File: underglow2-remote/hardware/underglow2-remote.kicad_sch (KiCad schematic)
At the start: 2 parts, among them J101 AFC01-S40FCA-00, U101 ATGM332D-5NR32

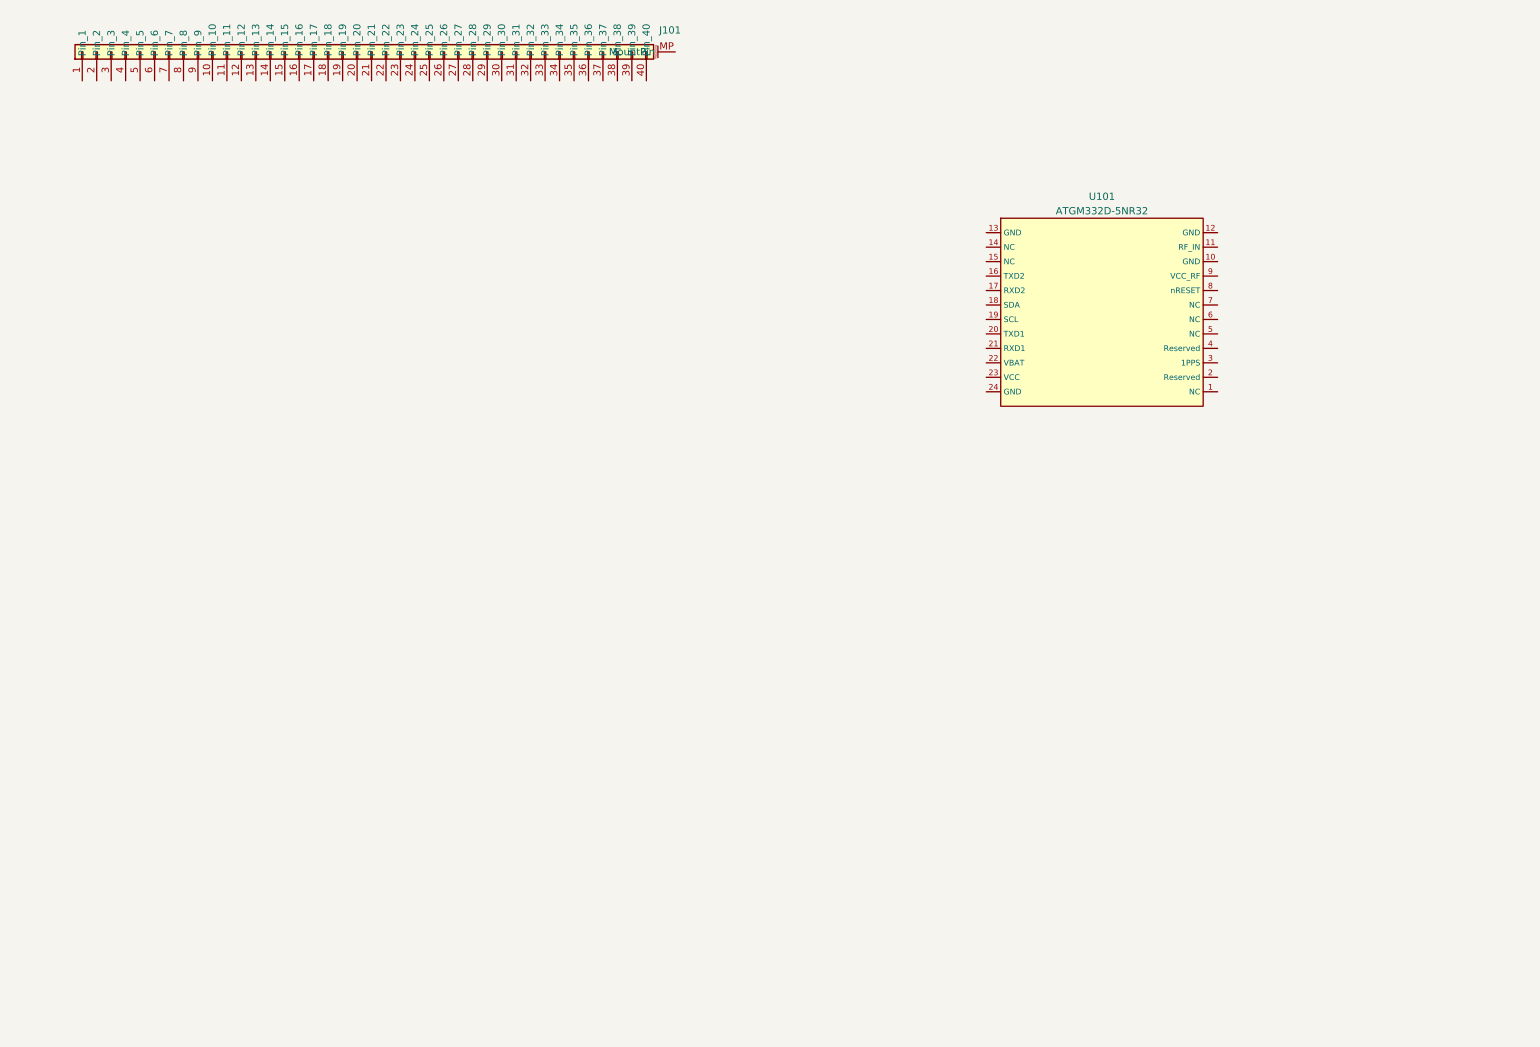
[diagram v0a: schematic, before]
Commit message: board layout testing for nds remote
Signed-off-by: Connor Rigby <connorr@hey.com>
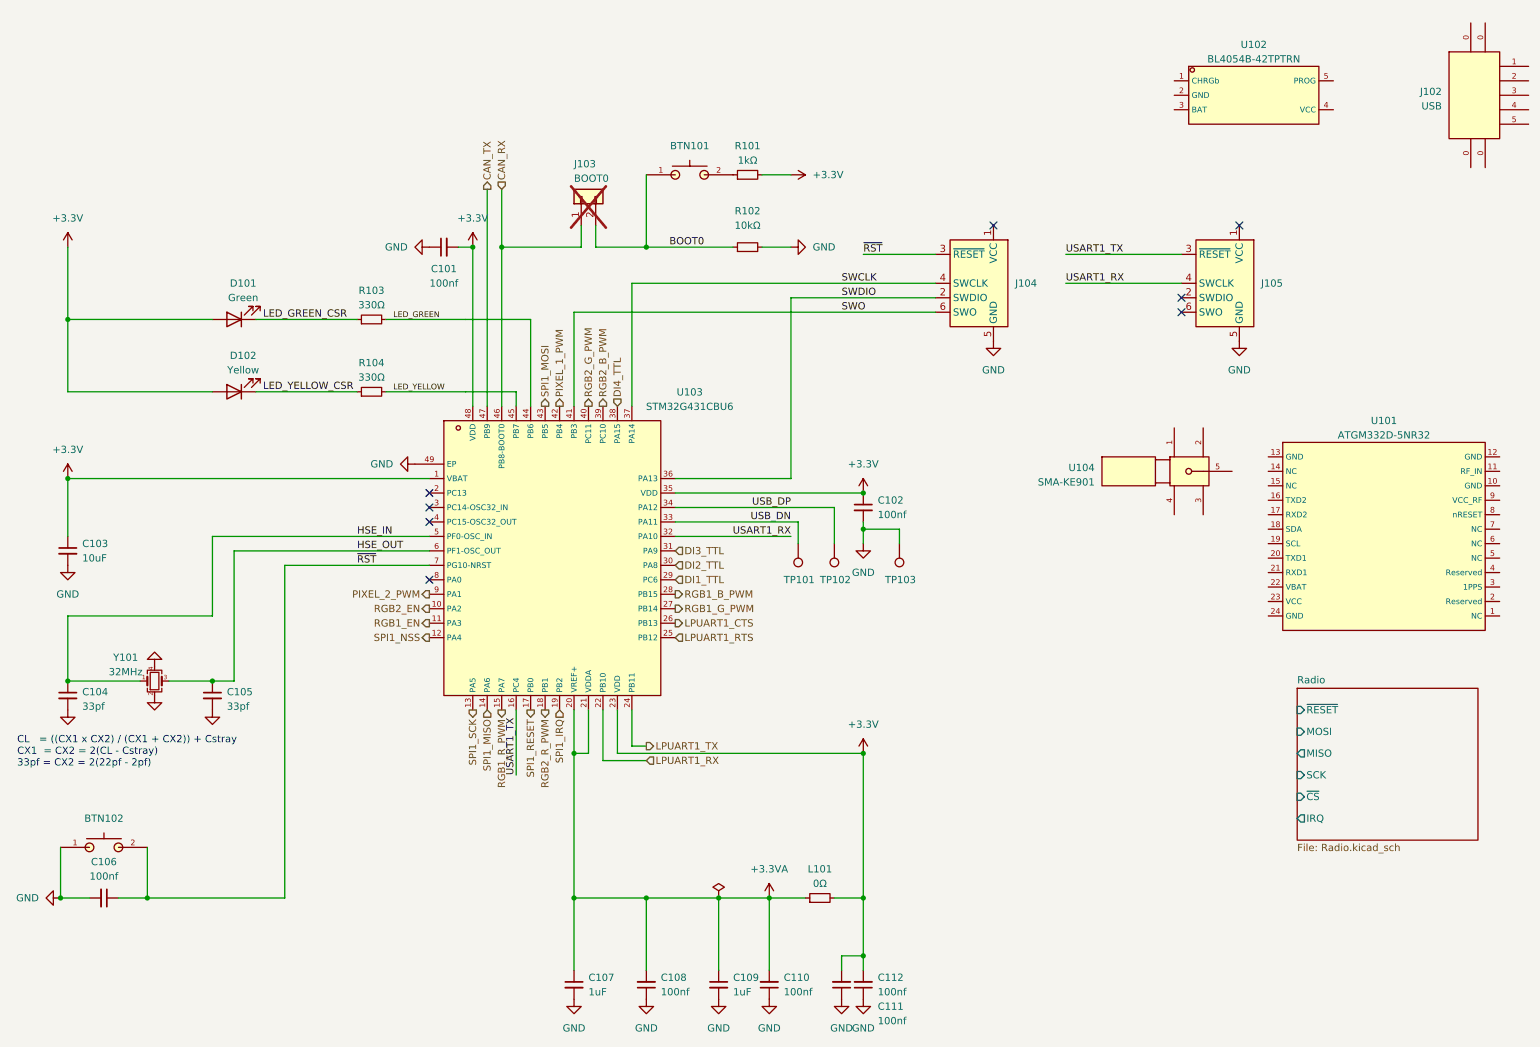
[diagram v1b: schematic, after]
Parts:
- removed J101: AFC01-S40FCA-00, LCSC_Connector:FPC-SMD_P0.50-40P_FGS-XJ-H2.0, symbol LCSC_Connector:AFC01-S40FCA-00
- added BTN101, BTN102: GT-TC029B-H025-L1N, Button:SW-SMD_L3.9-W3.0-P4.45, symbol LCSC_Tactile_Switch:GT-TC029B-H025-L1N
- added C101, C102, C106, C108, C110, C111, C112: C_0402_100nf_X7R, Capacitor_SMD:C_0402_1005Metric, symbol LCSC_Capacitor:C_0402_100nf_X7R
- added C103: C_0805_10u_X5R, Capacitor_SMD:C_0805_2012Metric, symbol LCSC_Capacitor:C_0805_10u_X5R
- added C104, C105: C_0402_33p_C0G, Capacitor_SMD:C_0402_1005Metric, symbol LCSC_Capacitor:C_0402_33p_C0G
- added C107, C109: C_0402_1u_X5R, Capacitor_SMD:C_0402_1005Metric, symbol LCSC_Capacitor:C_0402_1u_X5R
- added D101: LED_0603_GREEN, LED_SMD:LED_0603_1608Metric, symbol LCSC_LED:LED_0603_GREEN
- added D102: LED_0603_YELLOW, LED_SMD:LED_0603_1608Metric, symbol LCSC_LED:LED_0603_YELLOW
- added J102: u-m-m5ss-w-2, LCSC_Connector:MICRO-USB-SMD_MICRO-USB-13, symbol LCSC_Connector:u-m-m5ss-w-2
- added J103: BOOT0, Connector_PinHeader_2.54mm:PinHeader_1x02_P2.54mm_Vertical, symbol Connector_Generic:Conn_01x02
- added J104: Conn_ARM_SWD_TagConnect_TC2030-NL, Connector:Tag-Connect_TC2030-IDC-NL_2x03_P1.27mm_Vertical, symbol Connector:Conn_ARM_SWD_TagConnect_TC2030-NL
- added J105: Conn_ARM_SWD_TagConnect_TC2030, Connector:Tag-Connect_TC2030-IDC-FP_2x03_P1.27mm_Vertical, symbol Connector:Conn_ARM_SWD_TagConnect_TC2030
- added L101: R_0402_0, Resistor_SMD:R_0402_1005Metric, symbol LCSC_Resistor:R_0402_0
- added R101: R_0402_1k, Resistor_SMD:R_0402_1005Metric, symbol LCSC_Resistor:R_0402_1k
- added R102: R_0402_10k, Resistor_SMD:R_0402_1005Metric, symbol LCSC_Resistor:R_0402_10k
- added R103, R104: R_0603_330, Resistor_SMD:R_0603_1608Metric, symbol LCSC_Resistor:R_0603_330
- added TP101: DN, TestPoint:TestPoint_Pad_D1.0mm, symbol Connector:TestPoint
- added TP102: DP, TestPoint:TestPoint_Pad_D1.0mm, symbol Connector:TestPoint
- added TP103: GND, TestPoint:TestPoint_Pad_D1.0mm, symbol Connector:TestPoint
- added U102: BL4054B-42TPTRN, Package_TO_SOT_SMD:SOT-23-5, symbol LCSC_BatteryManagement:BL4054B-42TPTRN
- added U103: STM32G431CBU6, LCSC_Microcontroller:QFN50P700X700X60-49N, symbol LCSC_Microcontroller:STM32G431CBU6
- added U104: SMA-KE901, LCSC_Antenna:SMA-TH_SMA-KE901, symbol LCSC_Antenna:SMA-KE901
- added Y101: 32_Mhz, Crystal:Crystal_SMD_3225-4Pin_3.2x2.5mm, symbol LCSC_Crystal:32_Mhz
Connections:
- new net: BTN101.2, R101.1
- new net +3.3V: C101.2, C102.1, C103.1, C111.2, C112.2, D101.2 (A), D102.2 (A), L101.2, R101.2, U103.1 (VBAT), U103.23 (VDD), U103.35 (VDD), U103.48 (VDD)
- new net +3.3VA: C107.1, C108.2, C109.1, C110.2, L101.1, U103.20 (VREF+), U103.21 (VDDA)
- new net BOOT0: BTN101.1, J103.2 (Pin_2), R102.1
- new net CAN_RX: J103.1 (Pin_1), U103.46 (PB8-BOOT0)
- new net CAN_TX: U103.47 (PB9)
- new net DI1_TTL: U103.29 (PC6)
- new net DI2_TTL: U103.30 (PA8)
- new net DI3_TTL: U103.31 (PA9)
- new net DI4_TTL: U103.38 (PA15)
- new net GND: BTN102.1, C101.1, C102.2, C103.2, C104.2, C105.2, C106.2, C107.2, C108.1, C109.2, C110.1, C111.1, C112.1, J104.5 (GND), J105.5 (GND), R102.2, TP103.1, U103.49 (EP), Y101.2, Y101.4
- new net HSE_IN: C104.1, U103.5 (PF0-OSC_IN), Y101.1
- new net HSE_OUT: C105.1, U103.6 (PF1-OSC_OUT), Y101.3
- new net LED_GREEN: R103.2, U103.44 (PB6)
- new net LED_GREEN_CSR: D101.1 (K), R103.1
- new net LED_YELLOW: R104.2, U103.45 (PB7)
- new net LED_YELLOW_CSR: D102.1 (K), R104.1
- new net LPUART1_CTS: U103.26 (PB13)
- new net LPUART1_RTS: U103.25 (PB12)
- new net LPUART1_RX: U103.22 (PB10)
- new net LPUART1_TX: U103.24 (PB11)
- new net PIXEL_1_PWM: U103.42 (PB4)
- new net PIXEL_2_PWM: U103.9 (PA1)
- new net RGB1_B_PWM: U103.28 (PB15)
- new net RGB1_EN: U103.11 (PA3)
- new net RGB1_G_PWM: U103.27 (PB14)
- new net RGB1_R_PWM: U103.15 (PA7)
- new net RGB2_B_PWM: U103.39 (PC10)
- new net RGB2_EN: U103.10 (PA2)
- new net RGB2_G_PWM: U103.40 (PC11)
- new net RGB2_R_PWM: U103.18 (PB1)
- new net SPI1_IRQ: U103.19 (PB2)
- new net SPI1_MISO: U103.14 (PA6)
- new net SPI1_MOSI: U103.43 (PB5)
- new net SPI1_NSS: U103.12 (PA4)
- new net SPI1_RESET: U103.17 (PB0)
- new net SPI1_SCK: U103.13 (PA5)
- new net SWCLK: J104.4 (SWCLK), U103.37 (PA14)
- new net SWDIO: J104.2 (SWDIO), U103.36 (PA13)
- new net SWO: J104.6 (SWO), U103.41 (PB3)
- new net USART1_RX: J105.4 (SWCLK), U103.32 (PA10)
- new net USART1_TX: J105.3 (~{RESET}), U103.16 (PC4)
- new net USB_DN: TP101.1, U103.33 (PA11)
- new net USB_DP: TP102.1, U103.34 (PA12)
- new net ~{RST}: BTN102.2, C106.1, J104.3 (~{RESET}), U103.7 (PG10-NRST)
- no-connect marks 0 -> 8
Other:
- added sheet Radio (Radio.kicad_sch)
- note added: "CL = ((CX1 x CX2) / (CX1 + CX2)) + Cstray CX1 = CX2 = 2(CL - Cstray) 33pf = CX2 = 2(22pf - 2pf)"
- moved on the sheet: U101
